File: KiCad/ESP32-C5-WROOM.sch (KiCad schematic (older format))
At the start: 2 parts, among them U13 ESP32-C5-WROOM-1U-N8R8

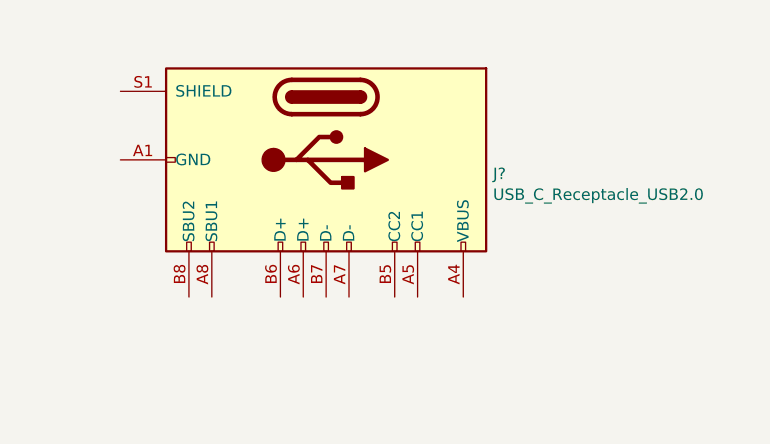
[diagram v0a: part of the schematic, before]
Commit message: Temporarily route USB_D- and USB_D+ signals from connector to ESP32-C5-WROOM module
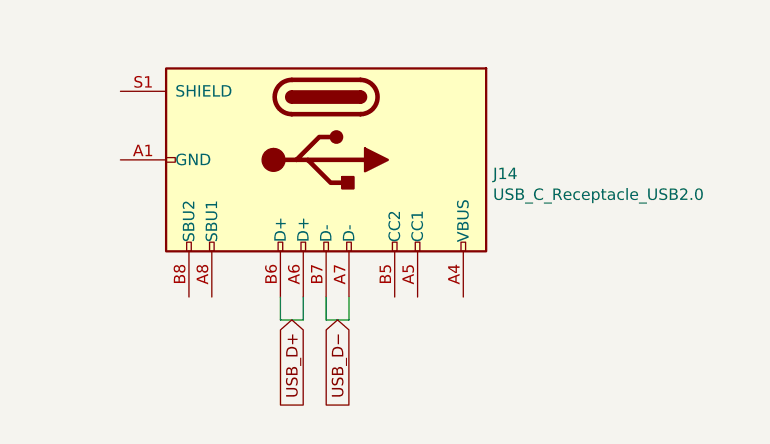
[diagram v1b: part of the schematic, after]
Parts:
- gave numbers to parts that had none: 1
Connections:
- net USB_D+: now also J14.A6 (D+), J14.B6 (D+)
- net USB_D−: now also J14.A7 (D-), J14.B7 (D-)
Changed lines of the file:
@@
 NoConn ~ 1650 3450
 $Comp
-L Connector:USB_C_Receptacle_USB2.0 J?
+L Connector:USB_C_Receptacle_USB2.0 J14
 U 1 1 6ABE0510
 P 2550 4450
-F 0 "J?" V 2611 5180 50  0000 L CNN
+F 0 "J14" V 2611 5180 50  0000 L CNN
 F 1 "USB_C_Receptacle_USB2.0" V 2702 5180 50  0000 L CNN
 F 2 "Connector_USB:USB_C_Receptacle_HRO_TYPE-C-31-M-12" H 2700 4450 50  0001 C CNN
@@
 	0    1    1    0
 $EndComp
+Text GLabel 2600 5150 3    50   Input ~ 0
+USB_D−
+Text GLabel 2400 5150 3    50   Input ~ 0
+USB_D+
+Wire Wire Line
+	2350 5050 2350 5150
+Wire Wire Line
+	2450 5050 2450 5150
+Wire Wire Line
+	2350 5150 2450 5150
+Wire Wire Line
+	2550 5050 2550 5150
+Wire Wire Line
+	2650 5050 2650 5150
+Wire Wire Line
+	2550 5150 2650 5150
 $EndSCHEMATC

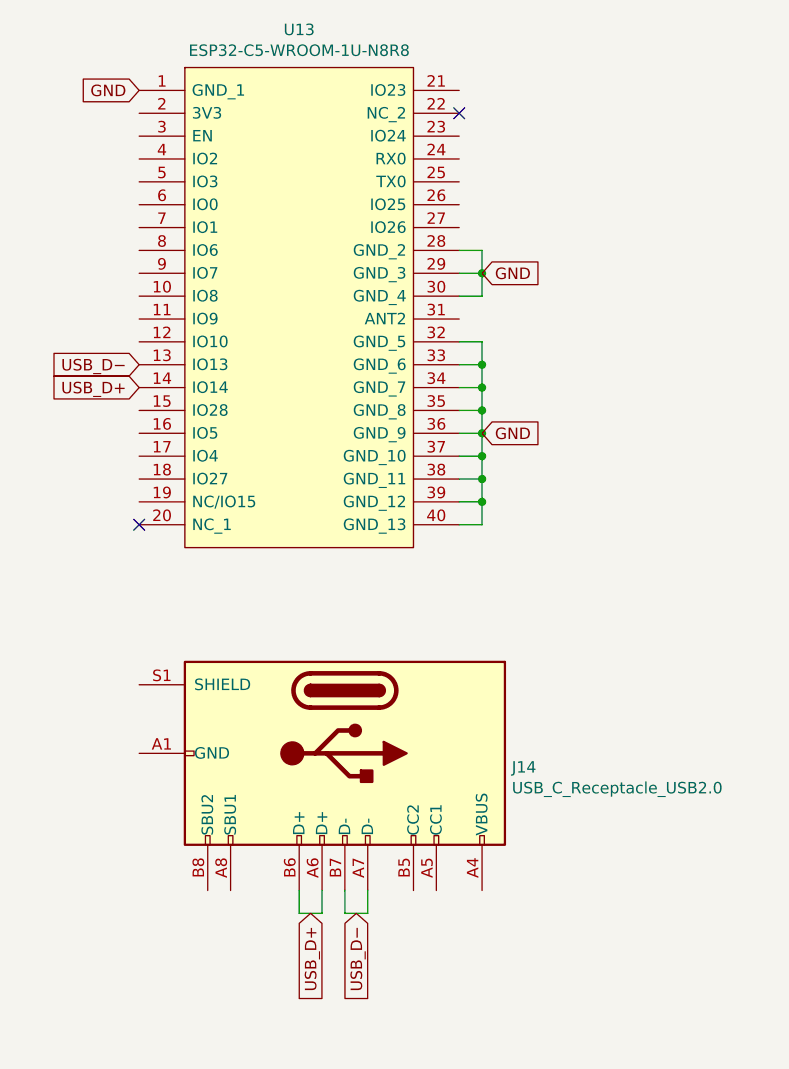
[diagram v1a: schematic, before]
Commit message: Replace TLV74312PDBV with TLV75533PDBVR (3.3V) and make it a supply to ESP32-C5 module (3V3_C5) only. Fixed external pull-up resistor network for 4-way dip switch signals. Rearranged JTAG TDI and TCK signals to have single pull-up/down resistor next to the pin-header.
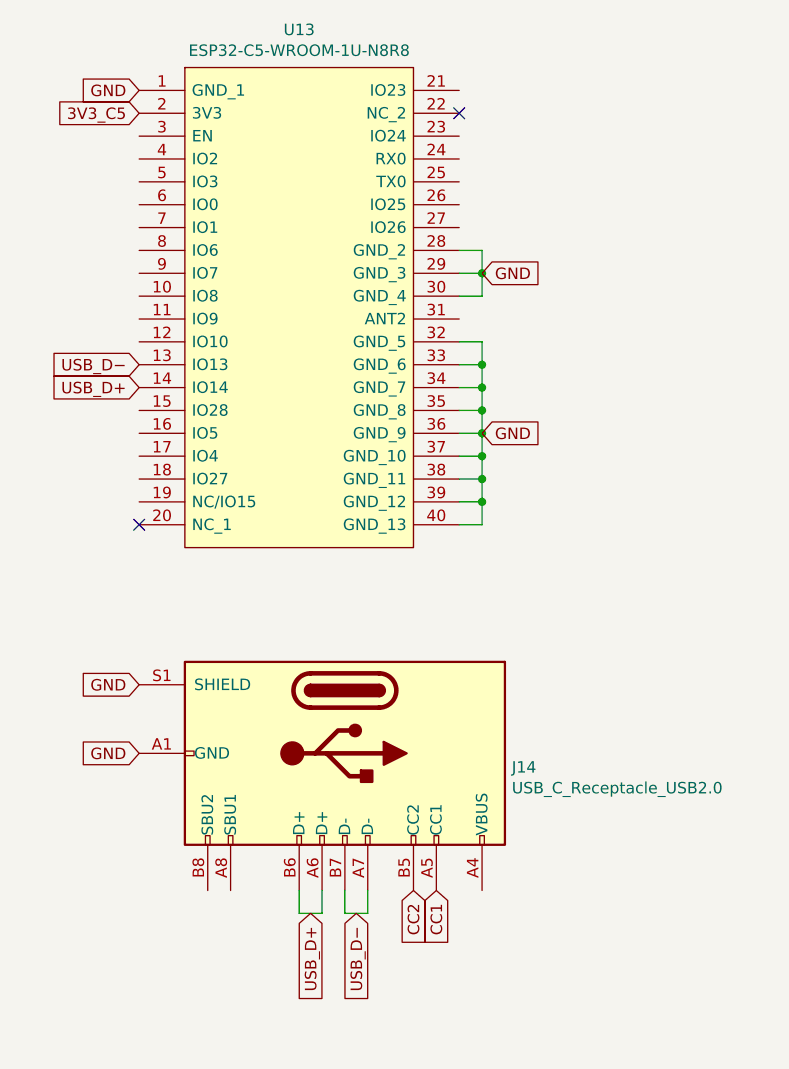
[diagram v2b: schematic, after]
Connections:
- net GND: now also J14.A1 (GND), J14.A12 (GND), J14.B1 (GND), J14.B12 (GND), J14.S1 (SHIELD)
- net 3V3_C5: now reaches U13.2 (3V3)
- net CC1: now reaches J14.A5 (CC1)
- net CC2: now reaches J14.B5 (CC2)
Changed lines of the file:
@@
 Wire Wire Line
 	2550 5150 2650 5150
+Text GLabel 2850 5050 3    50   Input ~ 0
+CC2
+Text GLabel 2950 5050 3    50   Input ~ 0
+CC1
+Text GLabel 1650 4450 0    50   Input ~ 0
+GND
+Text GLabel 1650 4150 0    50   Input ~ 0
+GND
+Text GLabel 1650 1650 0    50   Input ~ 0
+3V3_C5
 $EndSCHEMATC

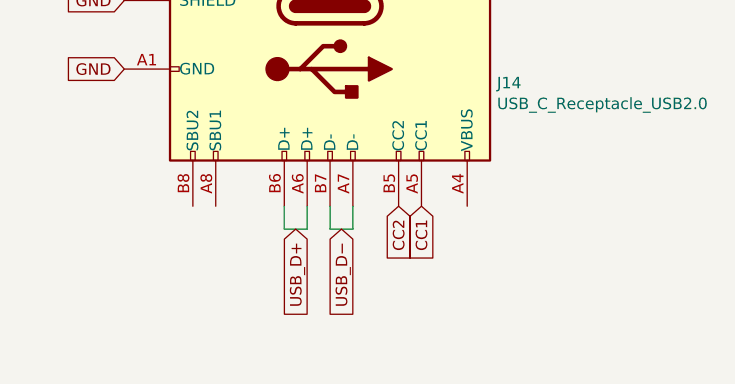
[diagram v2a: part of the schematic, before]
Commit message: Added 5.1k pull-down resistors for ESP32-C5 USB-C connector on CC1 and CC2
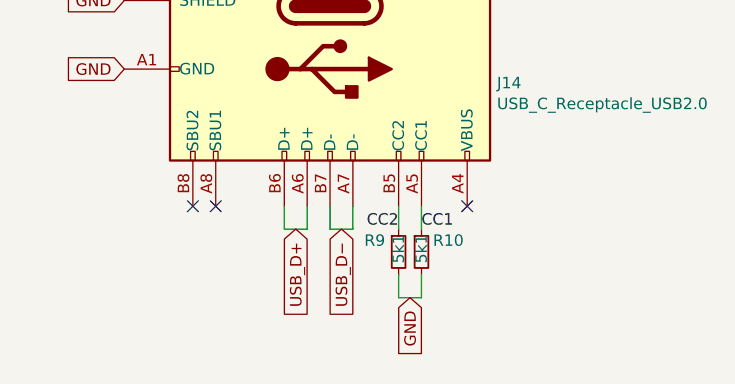
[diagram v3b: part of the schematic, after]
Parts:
- added R10, R9: 5k1, Resistor_SMD:R_0603_1608Metric_Pad0.98x0.95mm_HandSolder, symbol Device:R_Small
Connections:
- net CC1: now also R10.1
- net CC2: now also R9.1
- net GND: now also R10.2, R9.2
- no-connect marks 2 -> 5
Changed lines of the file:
@@
 Wire Wire Line
 	2550 5150 2650 5150
-Text GLabel 2850 5050 3    50   Input ~ 0
-CC2
-Text GLabel 2950 5050 3    50   Input ~ 0
-CC1
 Text GLabel 1650 4450 0    50   Input ~ 0
 GND
@@
 Text GLabel 1650 1650 0    50   Input ~ 0
 3V3_C5
+$Comp
+L Device:R_Small R9
+U 1 1 6AEB9B3F
+P 2850 5250
+F 0 "R9" H 2700 5300 50  0000 L CNN
+F 1 "5k1" V 2850 5200 50  0000 L CNN
+F 2 "Resistor_SMD:R_0603_1608Metric_Pad0.98x0.95mm_HandSolder" H 2850 5250 50  0001 C CNN
+F 3 "~" H 2850 5250 50  0001 C CNN
+	1    2850 5250
+	1    0    0    -1
+$EndComp
+Wire Wire Line
+	2850 5050 2850 5150
+Text Label 2850 5150 2    50   ~ 0
+CC2
+Text GLabel 2900 5450 3    50   Input ~ 0
+GND
+$Comp
+L Device:R_Small R10
+U 1 1 6AEC8E87
+P 2950 5250
+F 0 "R10" H 3000 5300 50  0000 L CNN
+F 1 "5k1" V 2950 5200 50  0000 L CNN
+F 2 "Resistor_SMD:R_0603_1608Metric_Pad0.98x0.95mm_HandSolder" H 2950 5250 50  0001 C CNN
+F 3 "~" H 2950 5250 50  0001 C CNN
+	1    2950 5250
+	1    0    0    -1
+$EndComp
+Wire Wire Line
+	2950 5050 2950 5150
+Text Label 2950 5150 0    50   ~ 0
+CC1
+Wire Wire Line
+	2850 5350 2850 5450
+Wire Wire Line
+	2950 5350 2950 5450
+Wire Wire Line
+	2850 5450 2950 5450
+NoConn ~ 1950 5050
+NoConn ~ 2050 5050
+NoConn ~ 3150 5050
 $EndSCHEMATC

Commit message: swap R9,R10 designators
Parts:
- renumbered R9 to R10, R10 to R9
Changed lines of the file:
@@
 3V3_C5
 $Comp
-L Device:R_Small R9
+L Device:R_Small R10
 U 1 1 6AEB9B3F
 P 2850 5250
-F 0 "R9" H 2700 5300 50  0000 L CNN
+F 0 "R10" V 2750 5150 50  0000 L CNN
 F 1 "5k1" V 2850 5200 50  0000 L CNN
 F 2 "Resistor_SMD:R_0603_1608Metric_Pad0.98x0.95mm_HandSolder" H 2850 5250 50  0001 C CNN
@@
 GND
 $Comp
-L Device:R_Small R10
+L Device:R_Small R9
 U 1 1 6AEC8E87
 P 2950 5250
-F 0 "R10" H 3000 5300 50  0000 L CNN
+F 0 "R9" V 3050 5150 50  0000 L CNN
 F 1 "5k1" V 2950 5200 50  0000 L CNN
 F 2 "Resistor_SMD:R_0603_1608Metric_Pad0.98x0.95mm_HandSolder" H 2950 5250 50  0001 C CNN

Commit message: temporarily route UART
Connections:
- net RX0: now reaches U13.24 (RX0)
- net TX0: now reaches U13.25 (TX0)
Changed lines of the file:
@@
 NoConn ~ 2050 5050
 NoConn ~ 3150 5050
+Text GLabel 3050 1850 2    50   Input ~ 0
+RX0
+Text GLabel 3050 1950 2    50   Output ~ 0
+TX0
 $EndSCHEMATC

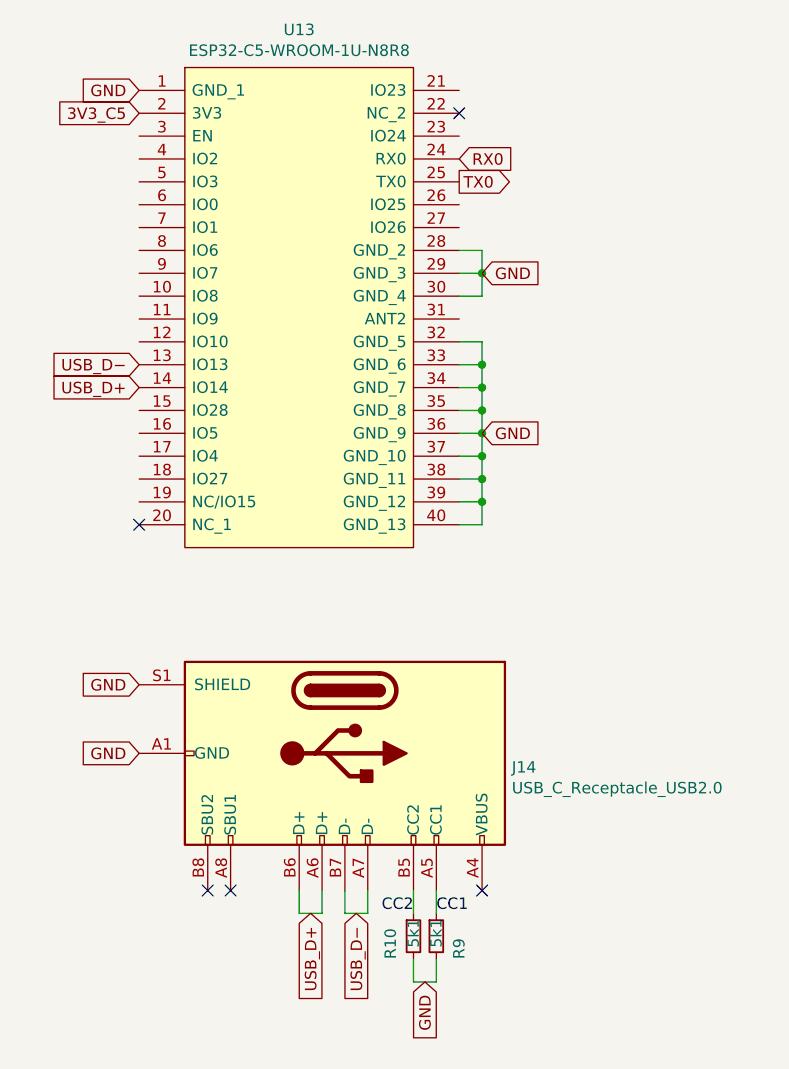
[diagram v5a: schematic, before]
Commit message: Switch to UART1 out from ESP32-C5 module, temporarily route /RTS,/CTS and also EN
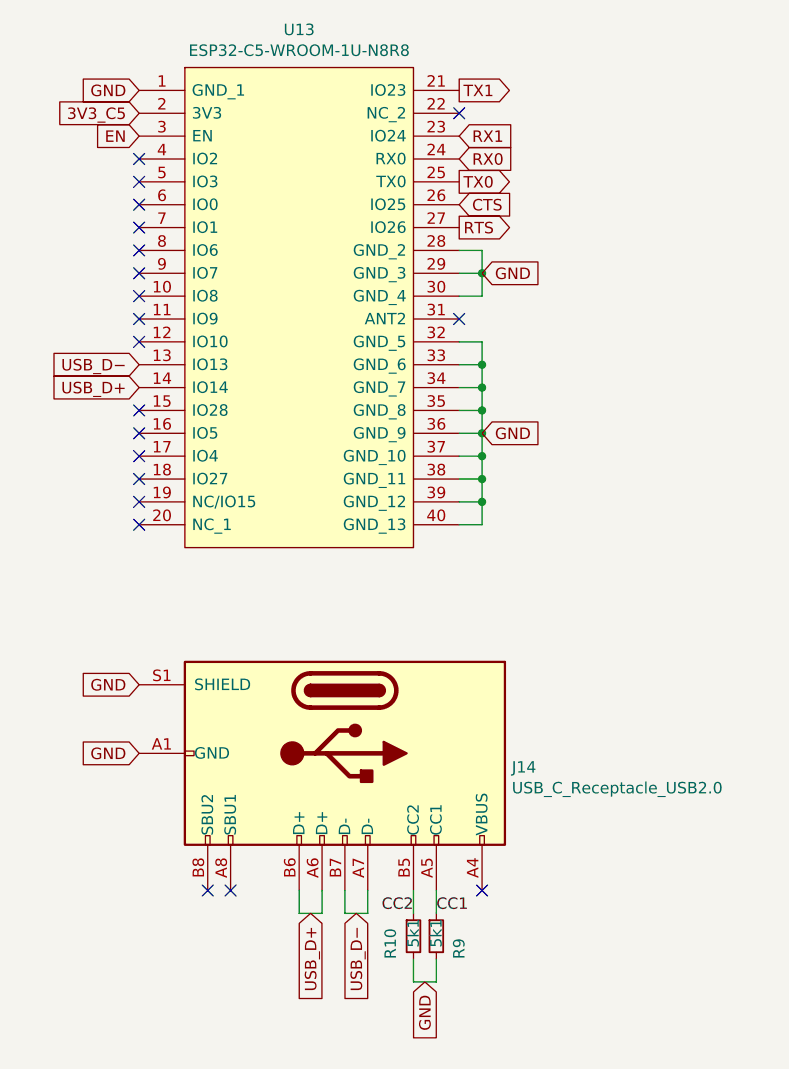
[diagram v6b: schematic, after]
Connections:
- net TX1: now reaches U13.21 (IO23)
- net RX1: now reaches U13.23 (IO24)
- net CTS: now reaches U13.26 (IO25)
- net RTS: now reaches U13.27 (IO26)
- net EN: now reaches U13.3 (EN)
- no-connect marks 5 -> 20
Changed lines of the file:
@@
 Text GLabel 3050 1950 2    50   Output ~ 0
 TX0
+Text GLabel 3050 2050 2    50   Input ~ 0
+CTS
+Text GLabel 3050 2150 2    50   Output ~ 0
+RTS
+Text GLabel 3050 1750 2    50   Input ~ 0
+RX1
+Text GLabel 3050 1550 2    50   Output ~ 0
+TX1
+Text GLabel 1650 1750 0    50   Input ~ 0
+EN
+NoConn ~ 3050 2550
+NoConn ~ 1650 1850
+NoConn ~ 1650 1950
+NoConn ~ 1650 2050
+NoConn ~ 1650 2150
+NoConn ~ 1650 2250
+NoConn ~ 1650 2350
+NoConn ~ 1650 2450
+NoConn ~ 1650 2550
+NoConn ~ 1650 2650
+NoConn ~ 1650 2950
+NoConn ~ 1650 3050
+NoConn ~ 1650 3150
+NoConn ~ 1650 3250
+NoConn ~ 1650 3350
 $EndSCHEMATC

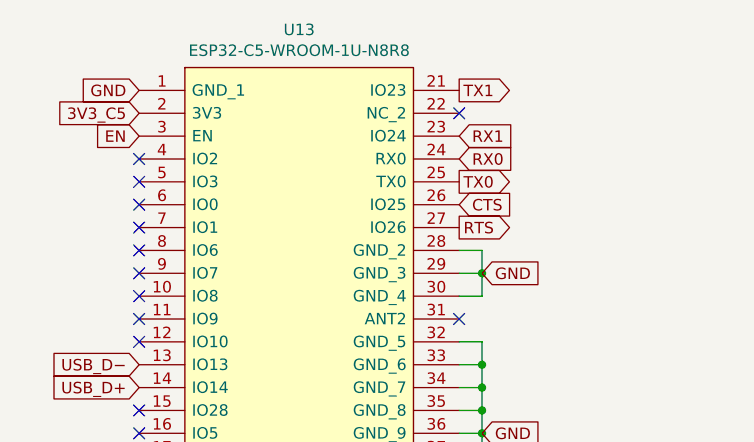
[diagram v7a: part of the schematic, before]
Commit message: Add SPI header and rename some signals coming from the ESP32-C5
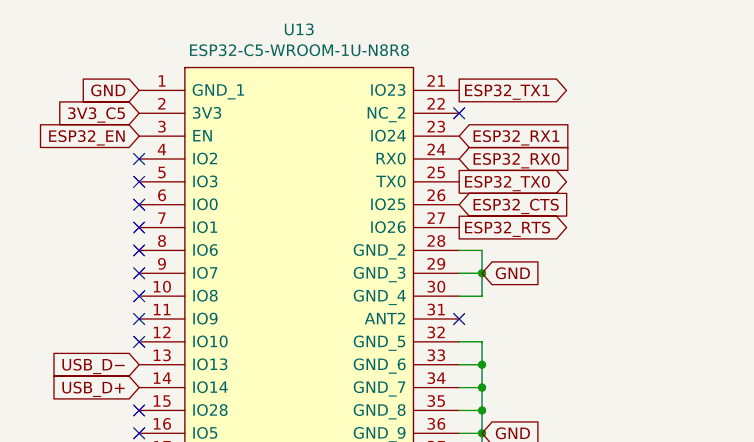
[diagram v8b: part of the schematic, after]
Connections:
- net CTS renamed ESP32_CTS
- net EN renamed ESP32_EN
- net RTS renamed ESP32_RTS
- net RX0 renamed ESP32_RX0
- net RX1 renamed ESP32_RX1
- net TX0 renamed ESP32_TX0
- net TX1 renamed ESP32_TX1
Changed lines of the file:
@@
 NoConn ~ 3150 5050
 Text GLabel 3050 1850 2    50   Input ~ 0
-RX0
+ESP32_RX0
 Text GLabel 3050 1950 2    50   Output ~ 0
-TX0
+ESP32_TX0
 Text GLabel 3050 2050 2    50   Input ~ 0
-CTS
+ESP32_CTS
 Text GLabel 3050 2150 2    50   Output ~ 0
-RTS
+ESP32_RTS
 Text GLabel 3050 1750 2    50   Input ~ 0
-RX1
+ESP32_RX1
 Text GLabel 3050 1550 2    50   Output ~ 0
-TX1
+ESP32_TX1
 Text GLabel 1650 1750 0    50   Input ~ 0
-EN
+ESP32_EN
 NoConn ~ 3050 2550
 NoConn ~ 1650 1850
